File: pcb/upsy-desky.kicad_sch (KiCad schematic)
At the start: 44 parts, among them J1 RJ45, J2 RJ45, J3 USB_C_ReceptacleUSB2.0, Q1 MMBT3904, Q2 MMBT3904, Q3 2N7002, Q4 2N7002, Q5 2N7002, Q6 2N7002, Q7 2N7002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

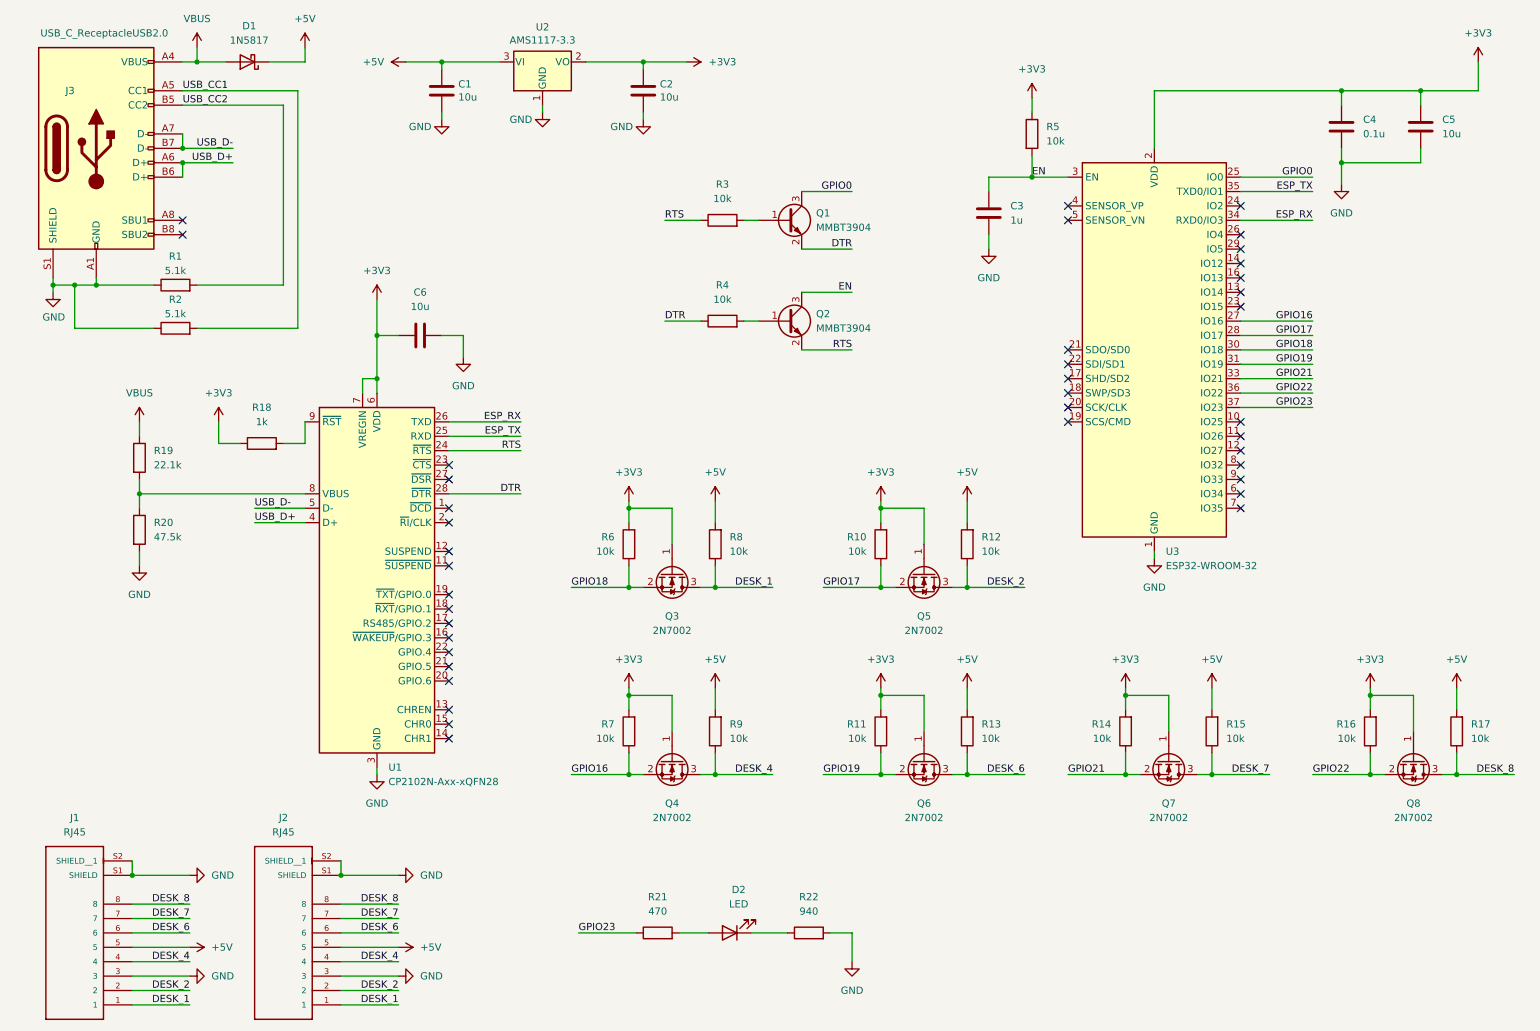
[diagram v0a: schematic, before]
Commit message: PCB: Change schematics to esp32 devkit
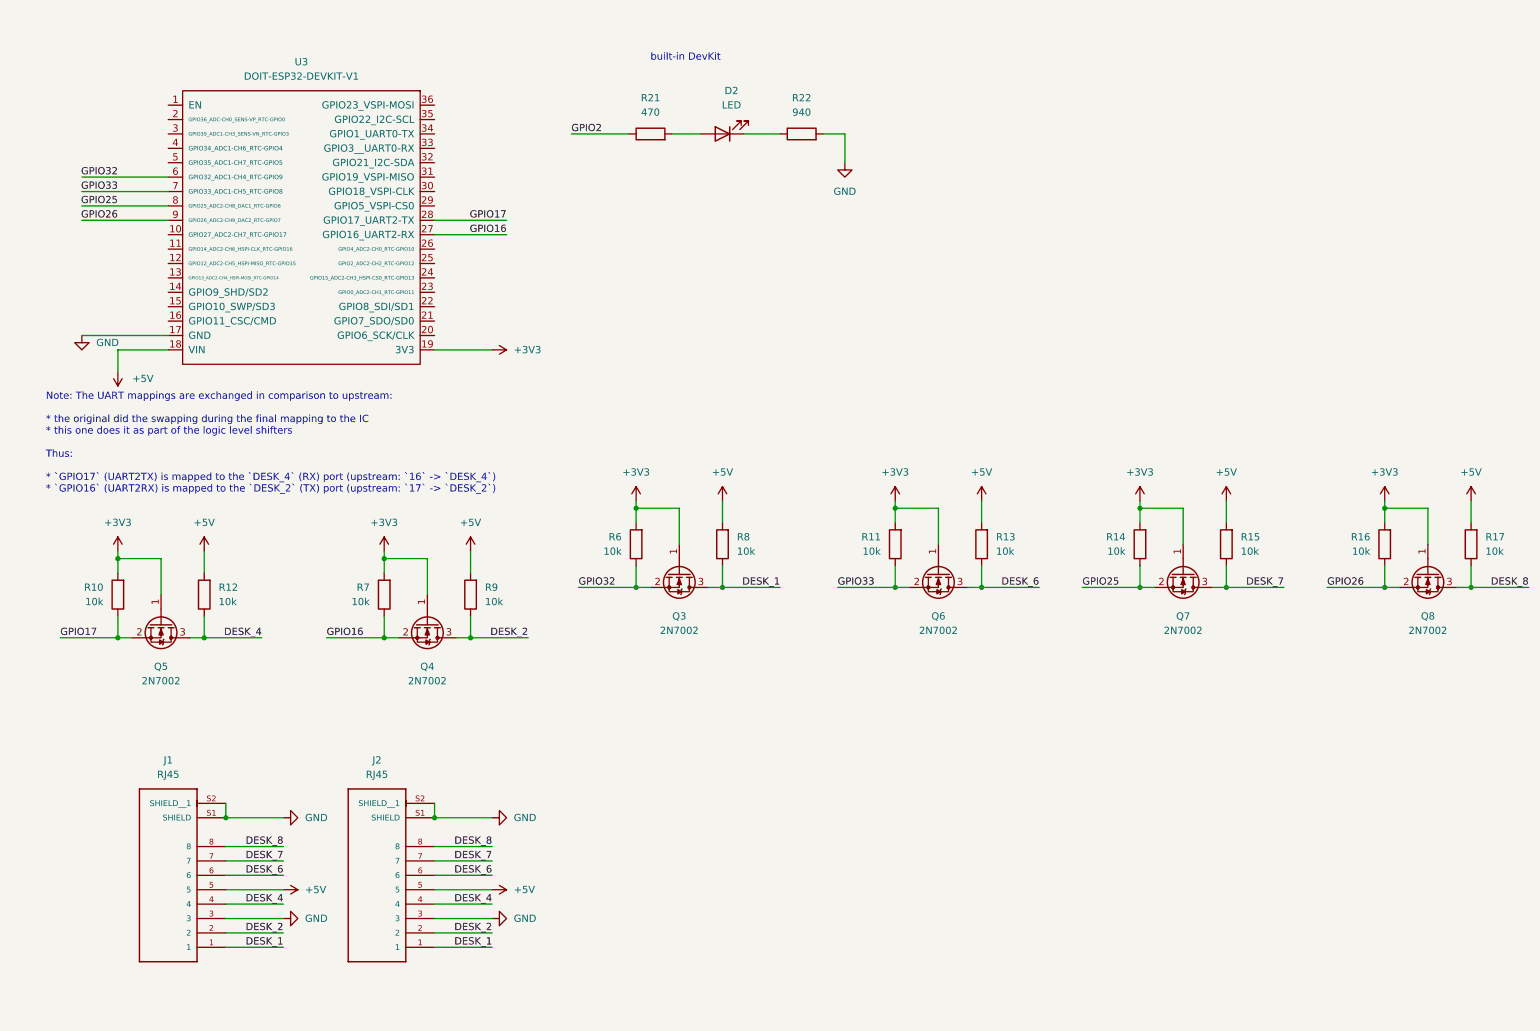
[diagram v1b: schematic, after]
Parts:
- removed C1, C2, C5, C6: 10u, Capacitor_SMD:C_0402_1005Metric, symbol Device:C
- removed C3: 1u, Capacitor_SMD:C_0402_1005Metric, symbol Device:C
- removed C4: 0.1u, Capacitor_SMD:C_0402_1005Metric, symbol Device:C
- removed D1: 1N5817, Diode_SMD:D_SOD-323, symbol Diode:1N5817
- removed J3: USB_C_ReceptacleUSB2.0, Connector_USB:USB_C_Receptacle_Palconn_UTC16-G, symbol Connector:USB_C_Receptacle_USB2.0
- removed Q1, Q2: MMBT3904, Package_TO_SOT_SMD:SOT-23, symbol Transistor_BJT:MMBT3904
- removed R1, R2: 5.1k, Resistor_SMD:R_0402_1005Metric, symbol Device:R
- removed R18: 1k, Resistor_SMD:R_0402_1005Metric, symbol Device:R
- removed R19: 22.1k, Resistor_SMD:R_0402_1005Metric, symbol Device:R
- removed R20: 47.5k, Resistor_SMD:R_0402_1005Metric, symbol Device:R
- removed R3, R4, R5: 10k, Resistor_SMD:R_0402_1005Metric, symbol Device:R
- removed U1: CP2102N-Axx-xQFN28, Package_DFN_QFN:QFN-28-1EP_5x5mm_P0.5mm_EP3.35x3.35mm, symbol Interface_USB:CP2102N-Axx-xQFN28
- removed U2: AMS1117-3.3, Package_TO_SOT_SMD:SOT-223-3_TabPin2, symbol Regulator_Linear:NCP1117-3.3_SOT223
- removed U3: ESP32-WROOM-32, RF_Module:ESP32-WROOM-32, symbol RF_Module:ESP32-WROOM-32
- added U3: DOIT-ESP32-DEVKIT-V1, symbol DOIT Esp32 DevKit v1:DOIT-ESP32-DEVKIT-V1
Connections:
- net +3V3: now also U3.19 (3V3)
- net +5V: now also U3.18 (VIN)
- net DESK_2: now also Q4.3 (D), R9.1; no longer Q5.3 (D), R12.1
- net DESK_4: now also Q5.3 (D), R12.1; no longer Q4.3 (D), R9.1
- net GND: now also U3.17 (GND)
- net GPIO16: now also U3.27 (GPIO16_UART2-RX)
- net GPIO17: now also U3.28 (GPIO17_UART2-TX)
- net GPIO18 renamed GPIO32
- net GPIO32: now also U3.6 (GPIO32_ADC1-CH4_RTC-GPIO9)
- net GPIO19 renamed GPIO33
- net GPIO33: now also U3.7 (GPIO33_ADC1-CH5_RTC-GPIO8)
- net GPIO21 renamed GPIO25
- net GPIO25: now also U3.8 (GPIO25_ADC2-CH8_DAC1_RTC-GPIO6)
- net GPIO22 renamed GPIO26
- net GPIO26: now also U3.9 (GPIO26_ADC2-CH9_DAC2_RTC-GPIO7)
- net GPIO23 renamed GPIO2
- no-connect marks 40 -> 0
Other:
- note added: "Note: The UART mappings are exchanged in comparison to upstream: * the original did the swapping during the final mapping to the IC * this one does it as part of the logic level shifters Thus: * `GPIO17` (UART2TX) is mapped to the `DESK_4` (RX) port (upstream: `16` -> `DESK_4`) * `GPIO16` (UART2RX) is mapped to the `DESK_2` (TX) port (upstream: `17` -> `DESK_2`)"
- note added: "built-in DevKit"
- moved on the sheet: D2, J1, J2, Q3, Q4, Q5, Q6, Q7, Q8, R10, R11, R12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
